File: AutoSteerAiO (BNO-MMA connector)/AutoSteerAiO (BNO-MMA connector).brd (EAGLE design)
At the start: 114.3 x 99.1 mm, 89 parts, among them J4 CONNECTOR 1x5 PINS, K4 CB1A-P-12V, T1 BC547, U1 VX7805-1000

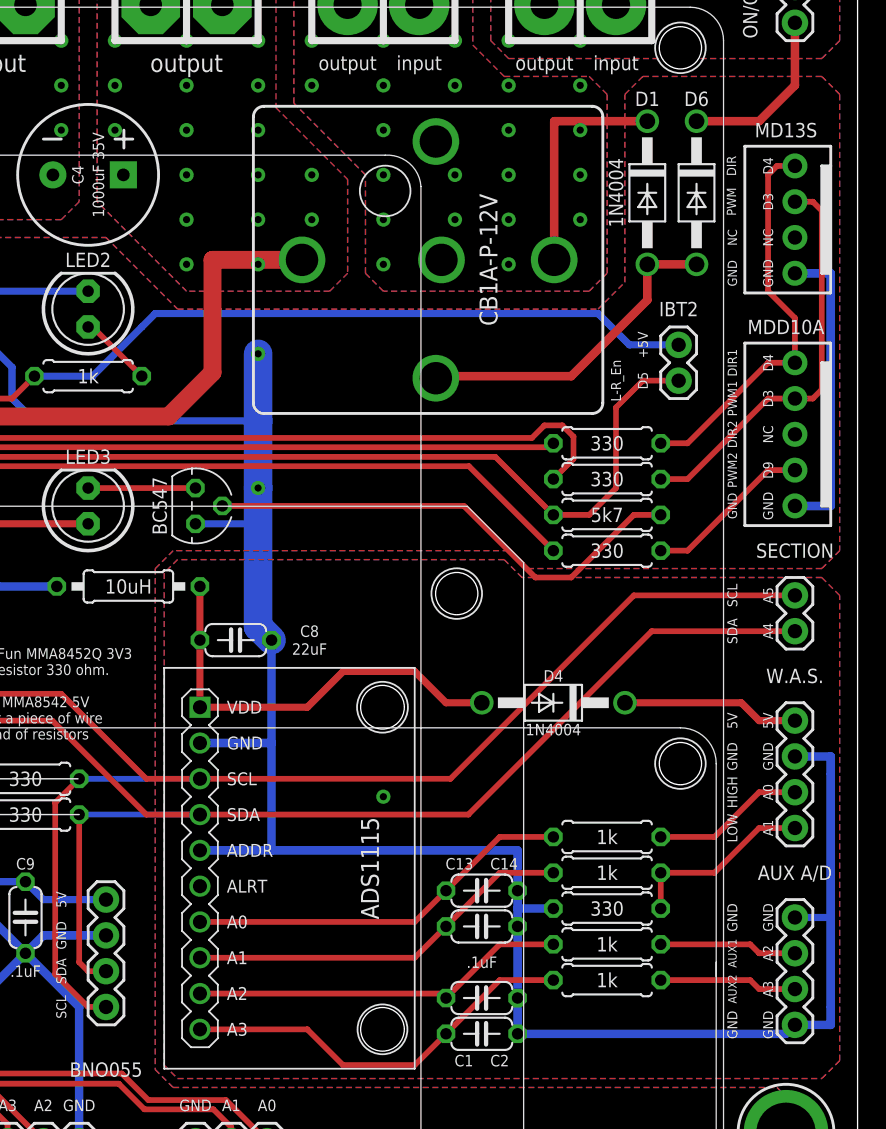
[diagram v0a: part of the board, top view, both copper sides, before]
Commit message: Add files via upload
One connector for all motor drivers
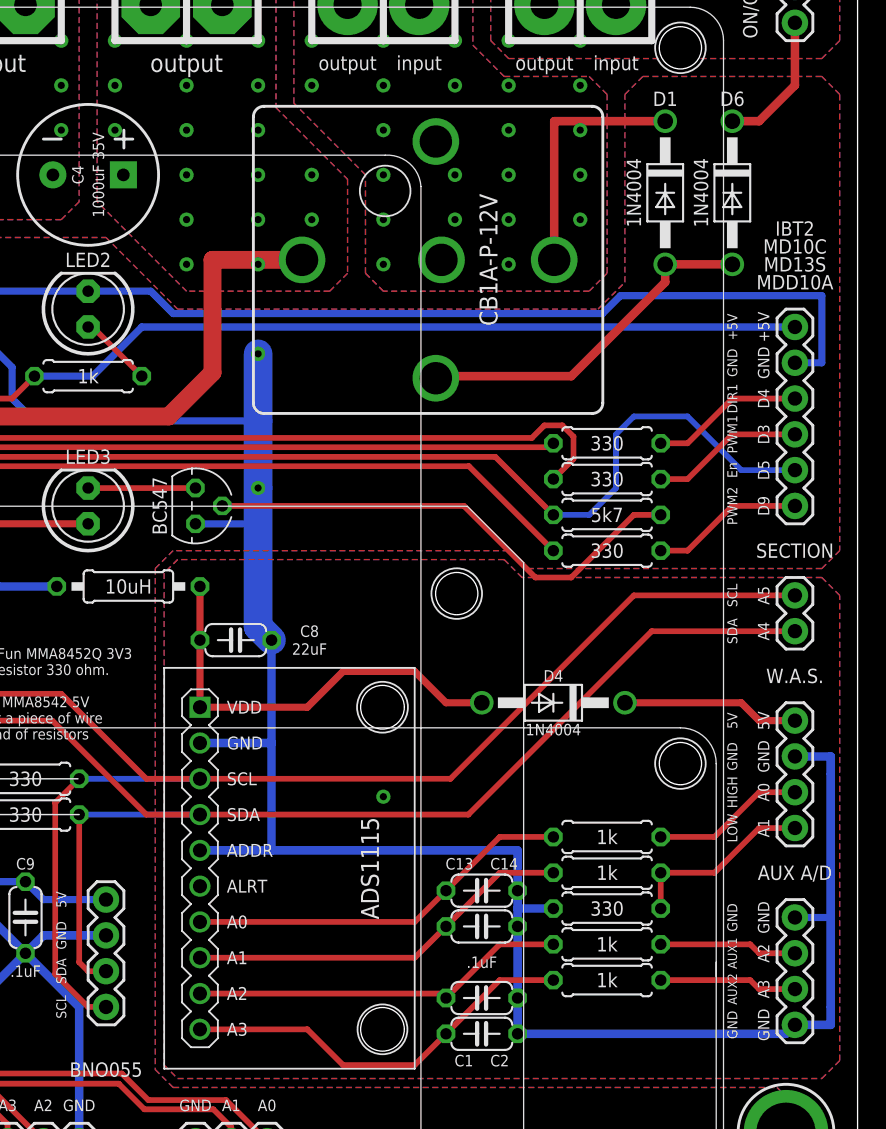
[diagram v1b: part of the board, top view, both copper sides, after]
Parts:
- removed D5: CONNECTOR 1x1 PIN, SparkFun-Connectors:1X02
- removed JP1: CONNECTOR 1x4 PINS, Header and Connector:2600-04
- J4: device Header and Connector:2600-05 -> SparkFun-Connectors:1X06
- moved D6 2.54 mm to (105.4, 71.8)
- moved D1 1.27 mm to (100.6, 71.8)
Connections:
- net +5V: now also J4.6; no longer D5.2
- net D5: now also J4.2; no longer D5.1
- net GND: now also J4.5; no longer J4.1, JP1.1
- net N$19: now also J4.4; no longer J4.5, JP1.4
- net N$20: now also J4.3; no longer J4.4, JP1.3
- net N$22: now also J4.1; no longer J4.2
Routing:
- net GND: track 580.0 -> 618.3 mm
- net N$20: track 28.9 -> 10.8 mm
- net N$19: track 28.2 -> 10.8 mm
- net D5: track 103.6 -> 111.2 mm
- net +5V: track 295.9 -> 302.9 mm
- net N$28: track 12.5 -> 9.94 mm
- net N$5: track 23.4 -> 25.2 mm
- net V+: track 16.4 -> 17.7 mm
- net N$22: track 11.9 -> 10.8 mm
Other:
- board text added: "D5"
- board text added: "En"
- board text removed: "DIR"
- board text removed: "DIR2"
- board text removed: "L-R_En"
- board text removed: "NC"
- board text removed: "PWM"

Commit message: Add files via upload
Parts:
- removed 15V1, 15V2, GND, GND30: WIREPAD4,16O1,6, wirepad:4,16O1,6
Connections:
- net +15V: no longer 15V1.1, 15V2.1
- net GND: no longer GND.1, GND30.1
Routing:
- net GND: vias 69 -> 71
- net +15V: vias 20 -> 22
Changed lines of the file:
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@@
 <setting verticaltext="up"/>
 </settings>
-<grid distance="50" unitdist="mil" unit="mil" style="lines" multiple="1" display="yes" altdistance="12.5" altunitdist="mil" altunit="mil"/>
+<grid distance="50" unitdist="mil" unit="mm" style="lines" multiple="1" display="yes" altdistance="12.5" altunitdist="mil" altunit="mil"/>
 <layers>
 <layer number="1" name="Top" color="4" fill="1" visible="yes" active="yes"/>
@@
 <attribute name="OC_NEWARK" value="unknown" x="109.855" y="86.36" size="1.778" layer="27" rot="R270" display="off"/>
 </element>
-<element name="15V1" library="wirepad" library_urn="urn:adsk.eagle:library:412" package="4,16O1,6" package3d_urn="urn:adsk.eagle:package:30843/1" value="WIREPAD4,16O1,6" x="69.215" y="85.09" smashed="yes" rot="R180">
-<attribute name="MF" value="" x="69.215" y="85.09" size="1.778" layer="27" rot="R180" display="off"/>
-<attribute name="MPN" value="" x="69.215" y="85.09" size="1.778" layer="27" rot="R180" display="off"/>
-<attribute name="OC_NEWARK" value="unknown" x="69.215" y="85.09" size="1.778" layer="27" rot="R180" display="off"/>
-</element>
-<element name="15V2" library="wirepad" library_urn="urn:adsk.eagle:library:412" package="4,16O1,6" package3d_urn="urn:adsk.eagle:package:30843/1" value="WIREPAD4,16O1,6" x="64.135" y="85.09" smashed="yes" rot="R180">
-<attribute name="MF" value="" x="64.135" y="85.09" size="1.778" layer="27" rot="R180" display="off"/>
-<attribute name="MPN" value="" x="64.135" y="85.09" size="1.778" layer="27" rot="R180" display="off"/>
-<attribute name="OC_NEWARK" value="unknown" x="64.135" y="85.09" size="1.778" layer="27" rot="R180" display="off"/>
-</element>
-<element name="GND" library="wirepad" library_urn="urn:adsk.eagle:library:412" package="4,16O1,6" package3d_urn="urn:adsk.eagle:package:30843/1" value="WIREPAD4,16O1,6" x="55.245" y="85.09" smashed="yes" rot="R180">
-<attribute name="MF" value="" x="55.245" y="85.09" size="1.778" layer="27" rot="R180" display="off"/>
-<attribute name="MPN" value="" x="55.245" y="85.09" size="1.778" layer="27" rot="R180" display="off"/>
-<attribute name="OC_NEWARK" value="unknown" x="55.245" y="85.09" size="1.778" layer="27" rot="R180" display="off"/>
-</element>
-<element name="GND30" library="wirepad" library_urn="urn:adsk.eagle:library:412" package="4,16O1,6" package3d_urn="urn:adsk.eagle:package:30843/1" value="WIREPAD4,16O1,6" x="50.165" y="85.09" smashed="yes" rot="R180">
-<attribute name="MF" value="" x="50.165" y="85.09" size="1.778" layer="27" rot="R180" display="off"/>
-<attribute name="MPN" value="" x="50.165" y="85.09" size="1.778" layer="27" rot="R180" display="off"/>
-<attribute name="OC_NEWARK" value="unknown" x="50.165" y="85.09" size="1.778" layer="27" rot="R180" display="off"/>
-</element>
 <element name="J4" library="SparkFun-Connectors" library_urn="urn:adsk.eagle:library:513" package="1X06" package3d_urn="urn:adsk.eagle:package:38009/1" value="CONNECTOR 1x5 PINS" x="109.855" y="49.53" smashed="yes" rot="R90">
 <attribute name="LABEL" value="" x="112.776" y="48.133" size="0.762" layer="51" font="vector" ratio="15" rot="R90" align="top-left"/>
@@
 <contactref element="C12" pad="1"/>
 <contactref element="C4" pad="-"/>
-<contactref element="GND30" pad="1"/>
-<contactref element="GND" pad="1"/>
 <contactref element="D3" pad="A"/>
 <contactref element="LED1" pad="K"/>
@@
 <via x="8.89" y="2.54" extent="1-16" drill="0.508"/>
 <via x="26.67" y="29.845" extent="1-16" drill="0.508"/>
-<via x="92.075" y="85.09" extent="1-16" drill="2" diameter="4.3" shape="square"/>
-<via x="97.155" y="85.09" extent="1-16" drill="2" diameter="4.3" shape="square"/>
+<via x="92.075" y="85.09" extent="1-16" drill="2.8" diameter="4.5" shape="square"/>
+<via x="97.155" y="85.09" extent="1-16" drill="2.8" diameter="4.5" shape="square"/>
 <contactref element="C5" pad="-"/>
 <via x="89.535" y="82.55" extent="1-16" drill="0.508"/>
@@
 <wire x1="109.855" y1="59.69" x2="111.76" y2="59.69" width="0.508" layer="16"/>
 <wire x1="111.76" y1="59.69" x2="111.76" y2="64.4525" width="0.508" layer="16"/>
+<via x="55.245" y="85.09" extent="1-16" drill="2.8" diameter="4.5" shape="square"/>
+<via x="50.165" y="85.09" extent="1-16" drill="2.8" diameter="4.5" shape="square"/>
 </signal>
 <signal name="D5">
@@
 </signal>
 <signal name="V+">
-<via x="83.185" y="85.09" extent="1-16" drill="2" diameter="4.3" shape="square"/>
-<via x="78.105" y="85.09" extent="1-16" drill="2" diameter="4.3" shape="square" alwaysstop="yes"/>
+<via x="83.185" y="85.09" extent="1-16" drill="2.8" diameter="4.5" shape="square"/>
+<via x="78.105" y="85.09" extent="1-16" drill="2.8" diameter="4.5" shape="square" alwaysstop="yes"/>
 <contactref element="K4" pad="87"/>
 <contactref element="K4" pad="85"/>
@@
 <signal name="+15V">
 <contactref element="C4" pad="+"/>
-<contactref element="15V1" pad="1"/>
-<contactref element="15V2" pad="1"/>
 <contactref element="R12" pad="1"/>
 <contactref element="R13" pad="1"/>
@@
 <wire x1="10.16" y1="18.415" x2="6.35" y2="18.415" width="0.6096" layer="1"/>
 <wire x1="6.35" y1="18.415" x2="5.08" y2="17.145" width="0.6096" layer="1"/>
+<via x="69.215" y="85.09" extent="1-16" drill="2.8" diameter="4.5" shape="square"/>
+<via x="64.135" y="85.09" extent="1-16" drill="2.8" diameter="4.5" shape="square"/>
 </signal>
 <signal name="HIGH">

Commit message: Add files via upload
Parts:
- moved U$11 1.91 mm to (78.1, 54.0)
- moved U$12 1.27 mm to (80.6, 48.9)
- moved AUX_A/D 0.64 mm to (109.2, 12.7)
- moved J4 0.64 mm to (109.2, 49.5)
- moved TO_SECTION 0.64 mm to (109.2, 43.2)
- moved WAS_D 0.64 mm to (109.2, 34.3)
- moved D1 0.63 mm to (100.0, 71.8)
- moved D6 0.63 mm to (104.8, 71.8)
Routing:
- net GND: track 618.3 -> 620.5 mm, vias 71 -> 78
- net +5V: track 302.9 -> 302.2 mm
- net SDA: track 100.8 -> 100.2 mm
- net SCL: track 106.8 -> 106.2 mm
- net N$22: track 10.8 -> 10.2 mm
- net N$21: track 12.6 -> 12.0 mm
- net N$20: track 10.8 -> 10.2 mm
- net N$19: track 10.8 -> 10.2 mm
- net N$11: track 9.79 -> 9.15 mm
- net N$10: track 9.79 -> 9.15 mm
- net LOW.: track 13.4 -> 12.7 mm
- net HIGH.: track 10.8 -> 10.2 mm
- net D5: track 111.2 -> 110.6 mm
- net V+: track 17.7 -> 17.1 mm
- net N$28: track 9.94 -> 10.6 mm
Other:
- board text added: "5V ok"
- board text added: "AutoSteer"
- board text added: "MOTOR DRIVER"
- board text added: "POWER"
- board text added: "WORK IMP SWITCH"
- board text removed: "IMP SWITCH"
- board text removed: "input"
